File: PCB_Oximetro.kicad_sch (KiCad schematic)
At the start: 8 parts, among them J1 USB_A, U1 LM2596T-3.3, U2 MAX30102

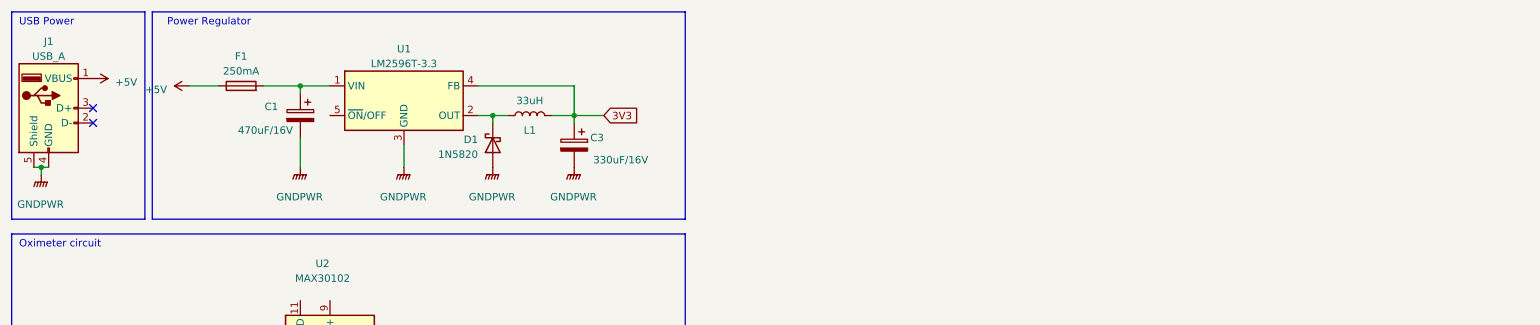
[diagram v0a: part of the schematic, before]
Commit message: Voltage regulators
Added voltage regulators for ESP-32 and MAX30102
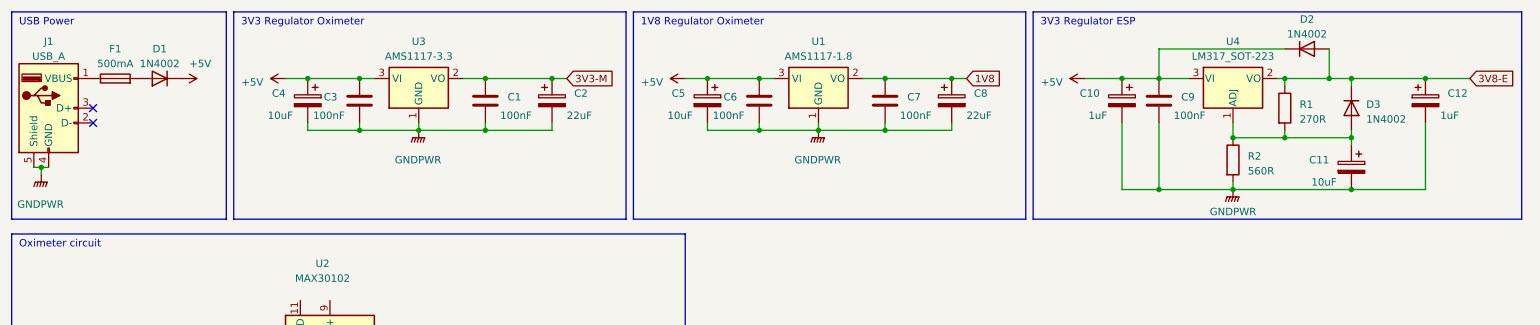
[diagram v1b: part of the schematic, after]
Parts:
- removed C1: 470uF/16V, symbol Device:C_Polarized
- removed C3: 330uF/16V, symbol Device:C_Polarized
- removed D1: 1N5820, Diode_THT:D_DO-201AD_P15.24mm_Horizontal, symbol Diode:1N5820
- removed L1: 33uH, symbol Device:L
- removed U1: LM2596T-3.3, Package_TO_SOT_THT:TO-220-5_Vertical, symbol Regulator_Switching:LM2596T-3.3
- added C1, C3, C6, C7, C9: 100nF, symbol Device:C
- added C10, C12: 1uF, symbol Device:C_Polarized
- added C11, C4, C5: 10uF, symbol Device:C_Polarized
- added C2, C8: 22uF, symbol Device:C_Polarized
- added D1, D2, D3: 1N4002, Diode_THT:D_DO-41_SOD81_P10.16mm_Horizontal, symbol Diode:1N4002
- added R1: 270R, Resistor_SMD:R_1206_3216Metric, symbol Device:R
- added R2: 560R, Resistor_SMD:R_1206_3216Metric, symbol Device:R
- added U1: AMS1117-1.8, Package_TO_SOT_SMD:SOT-223-3_TabPin2, symbol Regulator_Linear:AMS1117-1.8
- added U3: AMS1117-3.3, Package_TO_SOT_SMD:SOT-223-3_TabPin2, symbol Regulator_Linear:AMS1117-3.3
- added U4: LM317_SOT-223, Package_TO_SOT_SMD:SOT-223-3_TabPin2, symbol Regulator_Linear:LM317_SOT-223
- F1: value 250mA -> 500mA
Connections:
- net +5V: now also C10.1, C3.1, C4.1, C5.1, C6.1, C9.1, D1.1 (K), D2.1 (K), U1.3 (VI), U3.3 (VI), U4.3 (VI); no longer F1.1, J1.1 (VBUS)
- net GNDPWR: now also C1.2, C10.2, C11.2, C12.2, C2.2, C3.2, C4.2, C5.2, C6.2, C7.2, C8.2, C9.2, R2.2, U1.1 (GND), U3.1 (GND)
- net at F1.2: now also D1.2 (A)
- new net: C11.1, D3.2 (A), R1.2, R2.1, U4.1 (ADJ)
- new net: F1.1, J1.1 (VBUS)
- new net 1V8: C7.1, C8.1, U1.2 (VO)
- new net 3V3-M: C1.1, C2.1, U3.2 (VO)
- new net 3V8-E: C12.1, D2.2 (A), D3.1 (K), R1.1, U4.2 (VO)
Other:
- note added: "1V8 Regulator Oximeter"
- note added: "3V3 Regulator ESP"
- note added: "3V3 Regulator Oximeter"
- note removed: "Power Regulator"
- moved on the sheet: F1

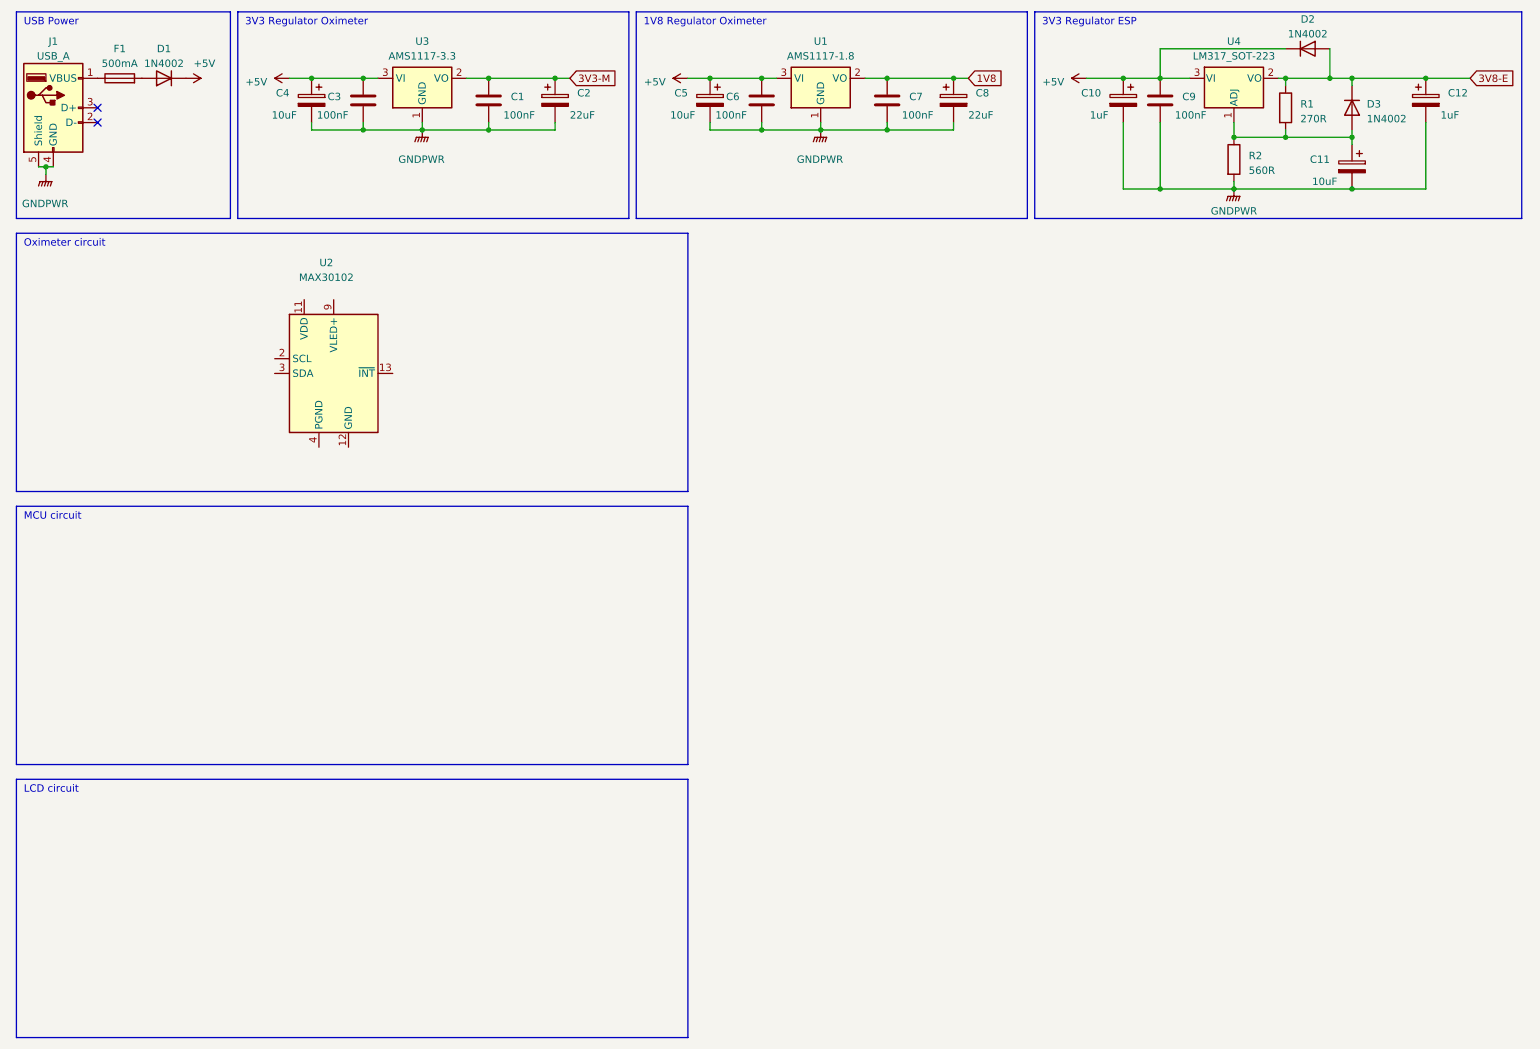
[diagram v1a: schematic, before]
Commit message: MCU, LCD and MAX30102
Added ESP32, LCD and MAX30102 schematics
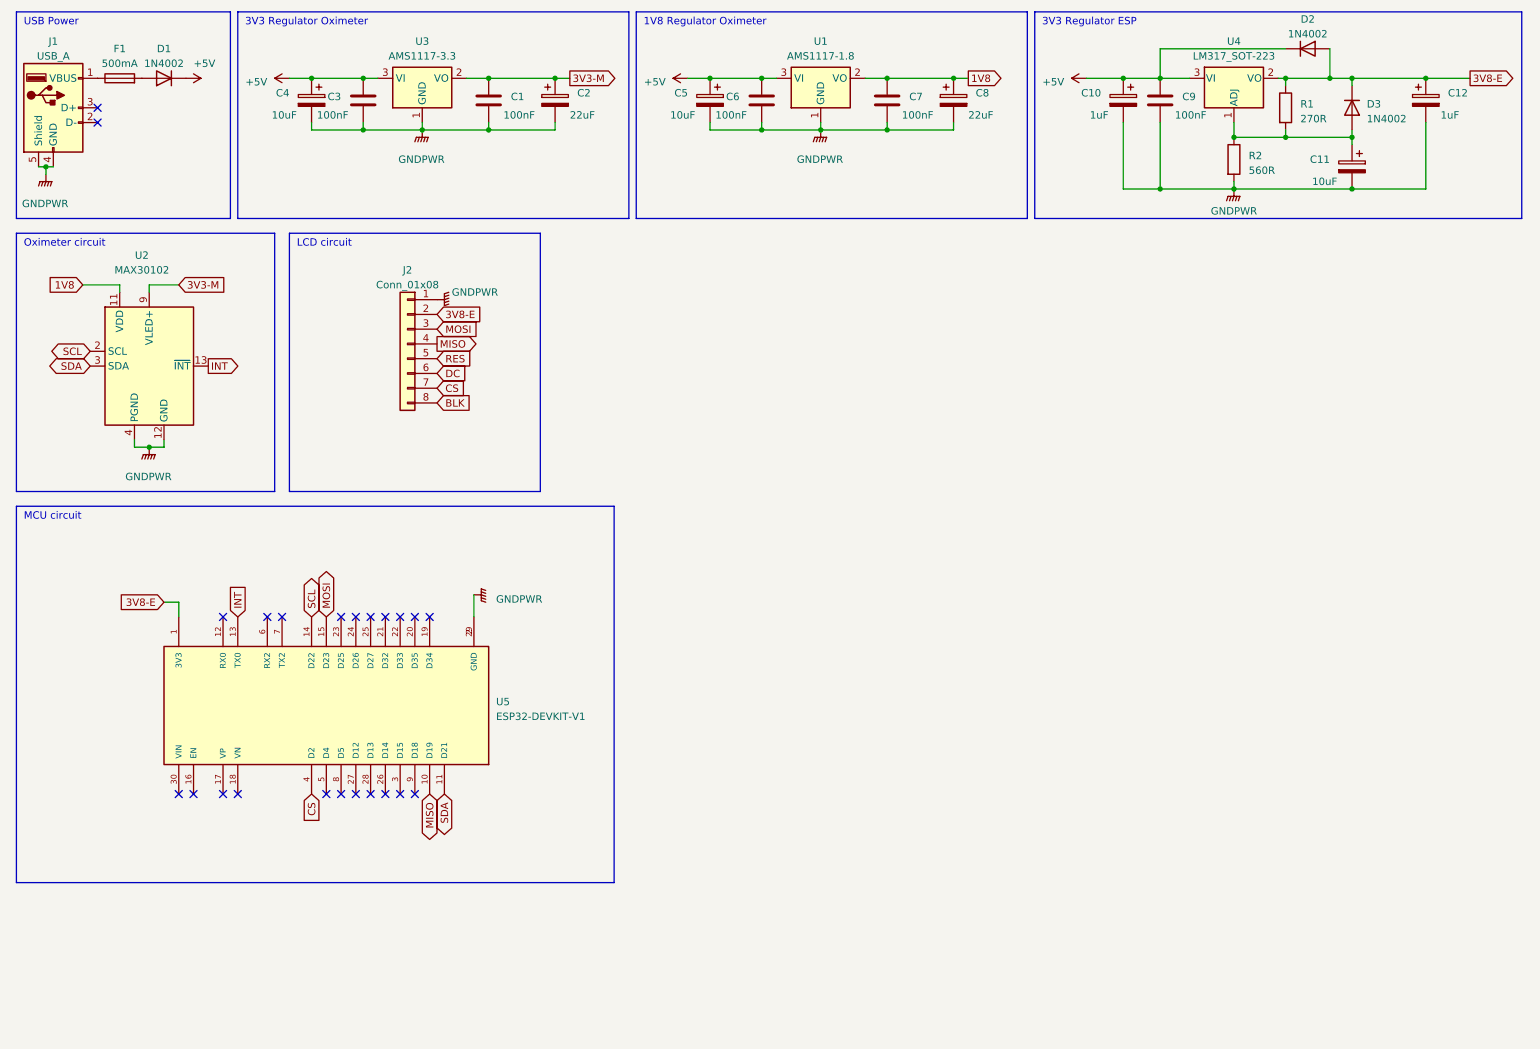
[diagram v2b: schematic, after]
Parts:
- added J2: Conn_01x08, Connector_PinHeader_2.54mm:PinHeader_1x08_P2.54mm_Vertical, symbol Connector_Generic:Conn_01x08
- added U5: ESP32-DEVKIT-V1, Espressif:MODULE_ESP32_DEVKIT_V1, symbol ESP32-DEVKIT-V1:ESP32-DEVKIT-V1
- C1, C3, C6, C7, C9: footprint (none) -> Capacitor_SMD:C_1206_3216Metric
- C10, C11, C12, C8: footprint (none) -> Capacitor_THT:CP_Radial_Tantal_D5.0mm_P2.50mm
- C4, C5: footprint (none) -> Capacitor_THT:CP_Radial_D5.0mm_P2.50mm
- F1: footprint (none) -> Fuse:Fuseholder_Cylinder-5x20mm_Stelvio-Kontek_PTF78_Horizontal_Open
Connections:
- net 1V8: now also U2.11 (VDD)
- net 3V3-M: now also U2.10 (VLED+), U2.9 (VLED+)
- net 3V8-E: now also J2.2 (Pin_2), U5.1 (3V3)
- net GNDPWR: now also U2.12 (GND), U2.4 (PGND), J2.1 (Pin_1), U5.2 (GND), U5.29 (GND)
- net INT: now reaches U2.13 (~{INT})
- net INT: now also U5.13 (TX0)
- net SCL: now reaches U2.2 (SCL)
- net SCL: now also U5.14 (D22)
- net SDA: now reaches U2.3 (SDA)
- net SDA: now also U5.11 (D21)
- new net BLK: J2.8 (Pin_8)
- new net CS: J2.7 (Pin_7), U5.4 (D2)
- new net DC: J2.6 (Pin_6)
- new net MISO: J2.4 (Pin_4), U5.10 (D19)
- new net MOSI: J2.3 (Pin_3), U5.15 (D23)
- new net RES: J2.5 (Pin_5)
- no-connect marks 2 -> 23
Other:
- moved on the sheet: U2

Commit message: 1st PCB
1st PCB layout
Regulators change
LCD pins adjust
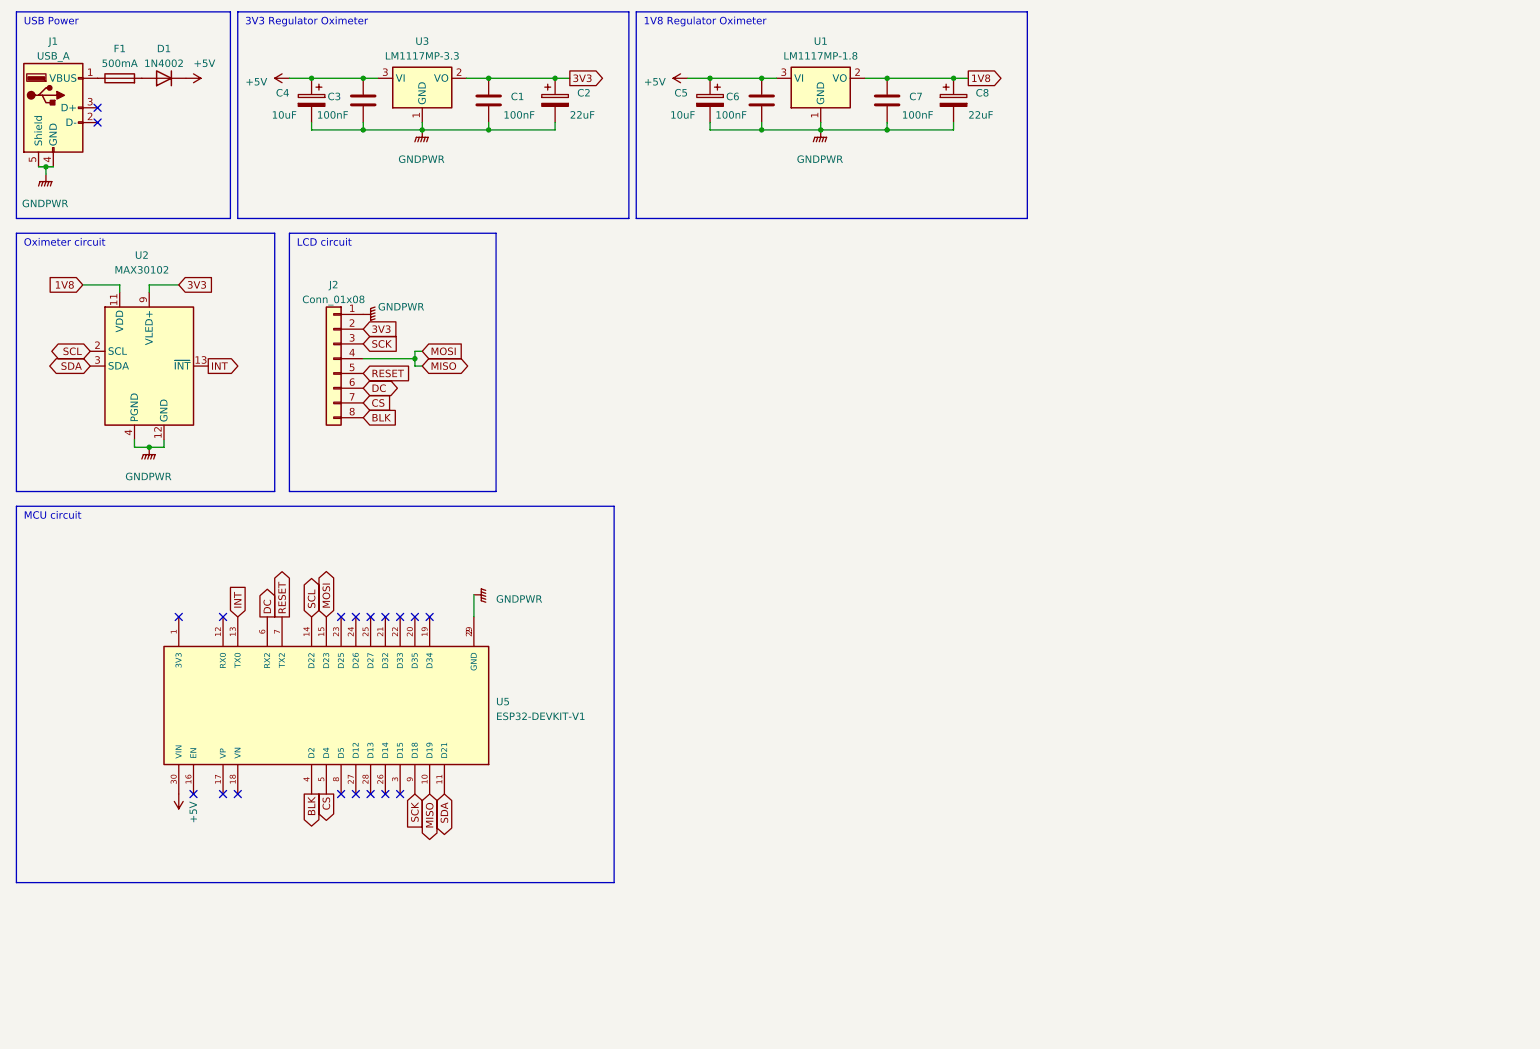
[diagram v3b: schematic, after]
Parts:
- removed C10, C12: 1uF, Capacitor_THT:CP_Radial_Tantal_D5.0mm_P2.50mm, symbol Device:C_Polarized
- removed C11: 10uF, Capacitor_THT:CP_Radial_Tantal_D5.0mm_P2.50mm, symbol Device:C_Polarized
- removed C9: 100nF, Capacitor_SMD:C_1206_3216Metric, symbol Device:C
- removed D2, D3: 1N4002, Diode_THT:D_DO-41_SOD81_P10.16mm_Horizontal, symbol Diode:1N4002
- removed R1: 270R, Resistor_SMD:R_1206_3216Metric, symbol Device:R
- removed R2: 560R, Resistor_SMD:R_1206_3216Metric, symbol Device:R
- removed U1: AMS1117-1.8, Package_TO_SOT_SMD:SOT-223-3_TabPin2, symbol Regulator_Linear:AMS1117-1.8
- removed U3: AMS1117-3.3, Package_TO_SOT_SMD:SOT-223-3_TabPin2, symbol Regulator_Linear:AMS1117-3.3
- removed U4: LM317_SOT-223, Package_TO_SOT_SMD:SOT-223-3_TabPin2, symbol Regulator_Linear:LM317_SOT-223
- added U1: LM1117MP-1.8, Package_TO_SOT_SMD:SOT-223-3_TabPin2, symbol Regulator_Linear:LM1117MP-1.8
- added U3: LM1117MP-3.3, Package_TO_SOT_SMD:SOT-223-3_TabPin2, symbol Regulator_Linear:LM1117MP-3.3
- C2: footprint (none) -> Capacitor_THT:CP_Radial_Tantal_D5.0mm_P2.50mm
- J1: footprint (none) -> Connector_USB:USB_A_Molex_67643_Horizontal
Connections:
- net RES is gone; now on net RESET: J2.5 (Pin_5)
- net +5V: now also U5.30 (VIN), U1.3 (VI), U3.3 (VI)
- net 1V8: now also U1.2 (VO)
- net BLK: now also U5.4 (D2)
- net CS: now also U5.5 (D4); no longer U5.4 (D2)
- net DC: now also U5.6 (RX2)
- net GNDPWR: now also U1.1 (GND), U3.1 (GND)
- net MISO: now also U5.15 (D23)
- net RESET: now reaches U5.7 (TX2)
- net SCK: now reaches U5.9 (D18)
- net SCK: now also J2.3 (Pin_3)
- net 3V3-M renamed 3V3
- net 3V3: now also J2.2 (Pin_2), U3.2 (VO)
- net 3V8-E: no longer names the net of U5.1 (3V3)
- net 3V8-E: no longer J2.2 (Pin_2)
- removed net MOSI: J2.3 (Pin_3), U5.15 (D23)
- no-connect marks 23 -> 19
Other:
- note removed: "3V3 Regulator ESP"
- moved on the sheet: J2

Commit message: PCB Layout
2nd PCB Layout (Without revision with professor)
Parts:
- J2: footprint Connector_PinHeader_2.54mm:PinHeader_1x08_P2.54mm_Vertical -> Connector_PinSocket_2.54mm:PinSocket_1x08_P2.54mm_Vertical
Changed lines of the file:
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@@
       (effects (font (size 1.27 1.27)))
     )
-    (property "Footprint" "Connector_PinHeader_2.54mm:PinHeader_1x08_P2.54mm_Vertical" (at 71.12 77.47 0)
+    (property "Footprint" "Connector_PinSocket_2.54mm:PinSocket_1x08_P2.54mm_Vertical" (at 71.12 77.47 0)
       (effects (font (size 1.27 1.27)) hide)
     )

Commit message: 3rd PCB Layout
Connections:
- net INT: now also U5.28 (D13); no longer U5.13 (TX0)
- net SCK: now also U5.14 (D22); no longer U5.9 (D18)
- net SCL: now also U5.27 (D12); no longer U5.14 (D22)
- net SDA: now also U5.26 (D14); no longer U5.11 (D21)
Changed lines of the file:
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@@
   (junction (at 135.89 29.21) (diameter 0) (color 0 0 0 0)
   )
-  (no_connect (at 74.93 152.4))
-  (no_connect (at 80.01 152.4))
+  (no_connect (at 85.09 152.4))
+  (no_connect (at 54.61 121.92))
   (no_connect (at 54.61 152.4))
   (no_connect (at 82.55 121.92))
@@
   (no_connect (at 72.39 121.92))
   (no_connect (at 46.99 152.4))
-  (no_connect (at 77.47 152.4))
+  (no_connect (at 90.17 152.4))
   (no_connect (at 77.47 121.92))
   (no_connect (at 80.01 121.92))
@@
     )
   )
-  (global_label "SCL" (shape bidirectional) (at 67.31 121.92 90) (fields_autoplaced)
-    (effects (font (size 1.27 1.27)) (justify left))
-    (property "Intersheetrefs" "${INTERSHEET_REFS}" (at 67.31 114.3953 90)
-      (effects (font (size 1.27 1.27)) (justify left) hide)
+  (global_label "SCL" (shape bidirectional) (at 74.93 152.4 270) (fields_autoplaced)
+    (effects (font (size 1.27 1.27)) (justify right))
+    (property "Intersheetrefs" "${INTERSHEET_REFS}" (at 74.93 159.9247 90)
+      (effects (font (size 1.27 1.27)) (justify right) hide)
     )
   )
@@
     )
   )
-  (global_label "SCK" (shape input) (at 85.09 152.4 270) (fields_autoplaced)
-    (effects (font (size 1.27 1.27)) (justify right))
-    (property "Intersheetrefs" "${INTERSHEET_REFS}" (at 85.09 159.0553 90)
-      (effects (font (size 1.27 1.27)) (justify right) hide)
+  (global_label "SCK" (shape input) (at 67.31 121.92 90) (fields_autoplaced)
+    (effects (font (size 1.27 1.27)) (justify left))
+    (property "Intersheetrefs" "${INTERSHEET_REFS}" (at 67.31 115.2647 90)
+      (effects (font (size 1.27 1.27)) (justify left) hide)
     )
   )
@@
     )
   )
-  (global_label "INT" (shape input) (at 54.61 121.92 90) (fields_autoplaced)
-    (effects (font (size 1.27 1.27)) (justify left))
-    (property "Intersheetrefs" "${INTERSHEET_REFS}" (at 54.61 116.1113 90)
-      (effects (font (size 1.27 1.27)) (justify left) hide)
-    )
-  )
-  (global_label "SDA" (shape bidirectional) (at 90.17 152.4 270) (fields_autoplaced)
-    (effects (font (size 1.27 1.27)) (justify right))
-    (property "Intersheetrefs" "${INTERSHEET_REFS}" (at 90.17 159.9852 90)
-      (effects (font (size 1.27 1.27)) (justify right) hide)
-    )
+  (global_label "INT" (shape input) (at 77.47 152.4 270) (fields_autoplaced)
+    (effects (font (size 1.27 1.27)) (justify right))
+    (property "Intersheetrefs" "${INTERSHEET_REFS}" (at 77.47 158.2087 90)
+      (effects (font (size 1.27 1.27)) (justify right) hide)
+    )
+  )
+  (global_label "SDA" (shape bidirectional) (at 80.01 152.4 270) (fields_autoplaced)
+    (effects (font (size 1.27 1.27)) (justify right))
+    (property "Intersheetrefs" "${INTERSHEET_REFS}" (at 80.01 159.9852 90)
+      (effects (font (size 1.27 1.27)) (justify right) hide)
+    )

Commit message: 4th PCB Layout
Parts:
- added C9: 10uF, Capacitor_THT:CP_Radial_D5.0mm_P2.50mm, symbol Device:C_Polarized
- added R1: 2K2, Resistor_SMD:R_1206_3216Metric, symbol Device:R
- added R2: 1K, Resistor_SMD:R_1206_3216Metric, symbol Device:R
- added SW1: SW_Push, Button_Switch_THT:SW_Tactile_SPST_Angled_PTS645Vx58-2LFS, symbol Switch:SW_Push
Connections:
- net +5V: now also R2.1
- net BLK: now also U5.15 (D23); no longer U5.4 (D2)
- net CS: now also U5.25 (D27); no longer U5.5 (D4)
- net DC: now also U5.24 (D26); no longer U5.6 (RX2)
- net GNDPWR: now also C9.2, R1.2
- net MISO: now also U5.19 (D34), U5.22 (D33); no longer U5.10 (D19), U5.15 (D23)
- net RESET: now also U5.23 (D25); no longer U5.7 (TX2)
- net SCK: now also U5.21 (D32); no longer U5.14 (D22)
- net BTT: now reaches U5.3 (D15)
- net BTT: now also C9.1, R1.1, SW1.2
- new net: R2.2, SW1.1
- no-connect marks 19 -> 18
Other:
- note added: "Button debounce"
